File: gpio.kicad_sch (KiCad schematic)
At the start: 3 parts, among them J3 Pyro Connectors

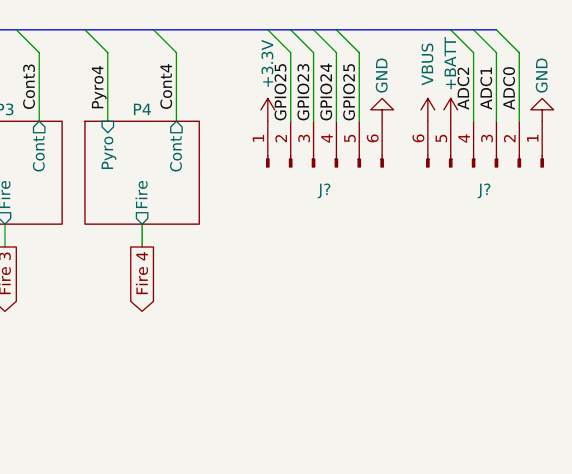
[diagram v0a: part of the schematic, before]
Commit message: Connected the sensors, flash chip, Need to connect the radio and GPS
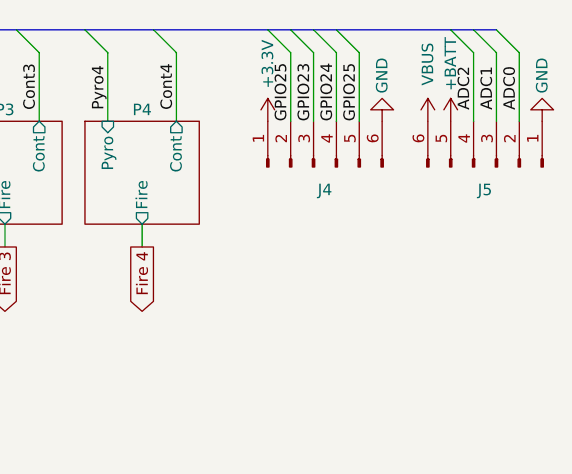
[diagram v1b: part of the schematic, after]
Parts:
- gave numbers to parts that had none: 2
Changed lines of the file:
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@@
   (symbol (lib_id "power:+BATT") (at 114.3 31.75 0) (unit 1)
     (in_bom yes) (on_board yes)
-    (property "Reference" "#PWR?" (id 0) (at 114.3 35.56 0)
+    (property "Reference" "#PWR063" (id 0) (at 114.3 35.56 0)
       (effects (font (size 1.27 1.27)) hide)
     )
@@
   (symbol (lib_id "Connector:Conn_01x06_Male") (at 99.06 36.83 90) (unit 1)
     (in_bom yes) (on_board yes) (fields_autoplaced)
-    (property "Reference" "J?" (id 0) (at 100.33 39.37 90))
+    (property "Reference" "J4" (id 0) (at 100.33 39.37 90))
     (property "Value" "Conn_01x05_Male" (id 1) (at 100.33 41.91 90)
       (effects (font (size 1.27 1.27)) hide)
@@
   (symbol (lib_id "power:+3.3V") (at 93.98 31.75 0) (unit 1)
     (in_bom yes) (on_board yes)
-    (property "Reference" "#PWR?" (id 0) (at 93.98 35.56 0)
+    (property "Reference" "#PWR060" (id 0) (at 93.98 35.56 0)
       (effects (font (size 1.27 1.27)) hide)
     )
@@
   (symbol (lib_id "power:+BATT") (at 35.56 104.14 90) (unit 1)
     (in_bom yes) (on_board yes)
-    (property "Reference" "#PWR057" (id 0) (at 39.37 104.14 0)
+    (property "Reference" "#PWR059" (id 0) (at 39.37 104.14 0)
       (effects (font (size 1.27 1.27)) hide)
     )
@@
   (symbol (lib_id "power:GND") (at 124.46 31.75 180) (unit 1)
     (in_bom yes) (on_board yes)
-    (property "Reference" "#PWR?" (id 0) (at 124.46 25.4 0)
+    (property "Reference" "#PWR064" (id 0) (at 124.46 25.4 0)
       (effects (font (size 1.27 1.27)) hide)
     )
@@
   (symbol (lib_id "power:GND") (at 106.68 31.75 180) (unit 1)
     (in_bom yes) (on_board yes)
-    (property "Reference" "#PWR?" (id 0) (at 106.68 25.4 0)
+    (property "Reference" "#PWR061" (id 0) (at 106.68 25.4 0)
       (effects (font (size 1.27 1.27)) hide)
     )
@@
   (symbol (lib_id "power:VBUS") (at 111.76 31.75 0) (unit 1)
     (in_bom yes) (on_board yes)
-    (property "Reference" "#PWR?" (id 0) (at 111.76 35.56 0)
+    (property "Reference" "#PWR062" (id 0) (at 111.76 35.56 0)
       (effects (font (size 1.27 1.27)) hide)
     )
@@
   (symbol (lib_id "Connector:Conn_01x06_Male") (at 119.38 36.83 270) (mirror x) (unit 1)
     (in_bom yes) (on_board yes) (fields_autoplaced)
-    (property "Reference" "J?" (id 0) (at 118.11 39.37 90))
+    (property "Reference" "J5" (id 0) (at 118.11 39.37 90))
     (property "Value" "Conn_01x05_Male" (id 1) (at 119.38 41.91 90)
       (effects (font (size 1.27 1.27)) hide)

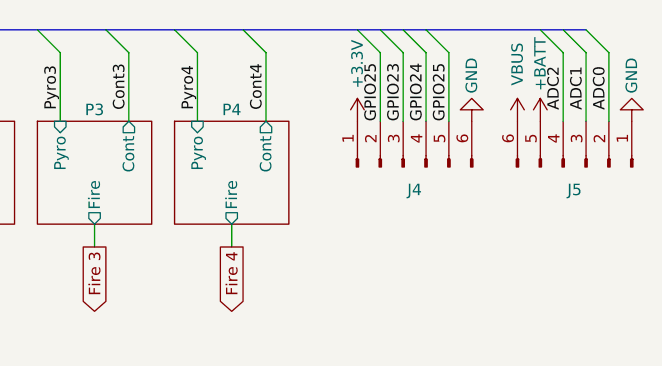
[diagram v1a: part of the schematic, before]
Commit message: Rearranged IO pins to make routing easier. Removed reset, changed BOOTSEL to button
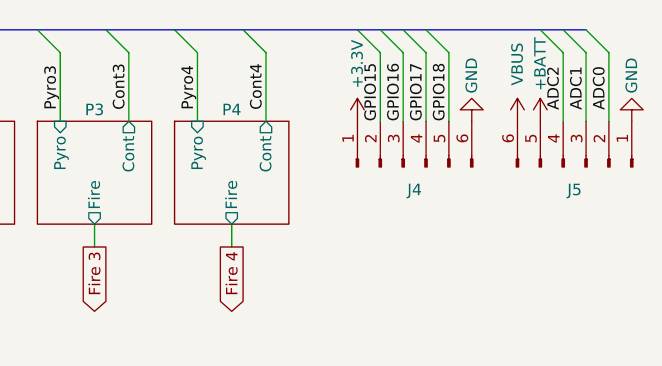
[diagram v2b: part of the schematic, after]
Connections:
- net GPIO23 renamed GPIO16
- net GPIO24 renamed GPIO17
- net GPIO25 renamed GPIO15
- net GPIO15: no longer J4.5 (Pin_5)
- new net GPIO18: J4.5 (Pin_5)
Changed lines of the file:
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@@
+    (effects (font (size 1.27 1.27)) (justify left bottom))
+  )
+  (label "GPIO17" (at 101.6 31.75 90)
+    (effects (font (size 1.27 1.27)) (justify left bottom))
+  )
+  (label "GPIO15" (at 96.52 31.75 90)
     (effects (font (size 1.27 1.27)) (justify left bottom))
   )
@@
     (effects (font (size 1.27 1.27)) (justify left bottom))
   )
-  (label "GPIO25" (at 96.52 31.75 90)
+  (label "GPIO16" (at 99.06 31.75 90)
     (effects (font (size 1.27 1.27)) (justify left bottom))
   )
@@
     (effects (font (size 1.27 1.27)) (justify right bottom))
   )
-  (label "GPIO24" (at 101.6 31.75 90)
-    (effects (font (size 1.27 1.27)) (justify left bottom))
-  )
   (label "Cont1" (at 38.1 30.48 90)
-    (effects (font (size 1.27 1.27)) (justify left bottom))
-  )
-  (label "GPIO25" (at 104.14 31.75 90)
     (effects (font (size 1.27 1.27)) (justify left bottom))
   )
@@
     (effects (font (size 1.27 1.27)) (justify left bottom))
   )
+  (label "GPIO18" (at 104.14 31.75 90)
+    (effects (font (size 1.27 1.27)) (justify left bottom))
+  )
   (label "Cont4" (at 83.82 30.48 90)
     (effects (font (size 1.27 1.27)) (justify left bottom))
   )
-  (label "GPIO23" (at 99.06 31.75 90)
-    (effects (font (size 1.27 1.27)) (justify left bottom))
-  )

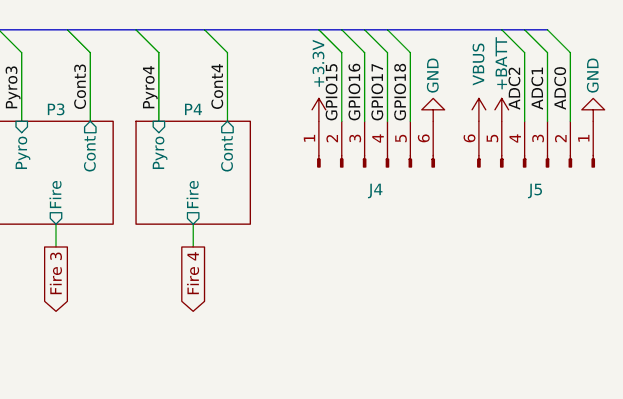
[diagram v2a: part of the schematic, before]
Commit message: Removed GPIO, changed footprints
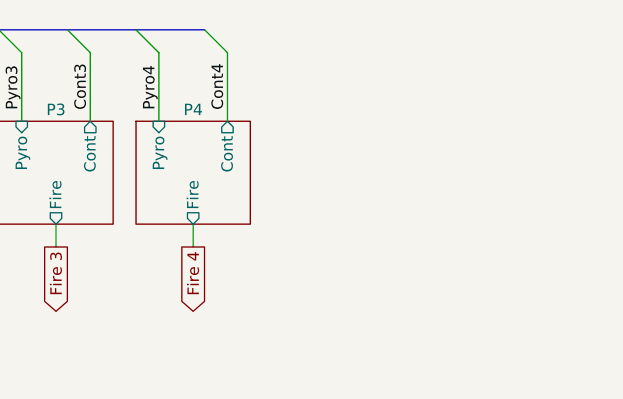
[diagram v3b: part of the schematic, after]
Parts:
- removed J4, J5: Conn_01x05_Male, symbol Connector:Conn_01x06_Male
- J3: footprint Connector_Phoenix_MC_HighVoltage:PhoenixContact_MCV_1,5_10-G-5.08_1x10_P5.08mm_Vertical -> YAR_Connectors:ScrewTerm_2.54x10

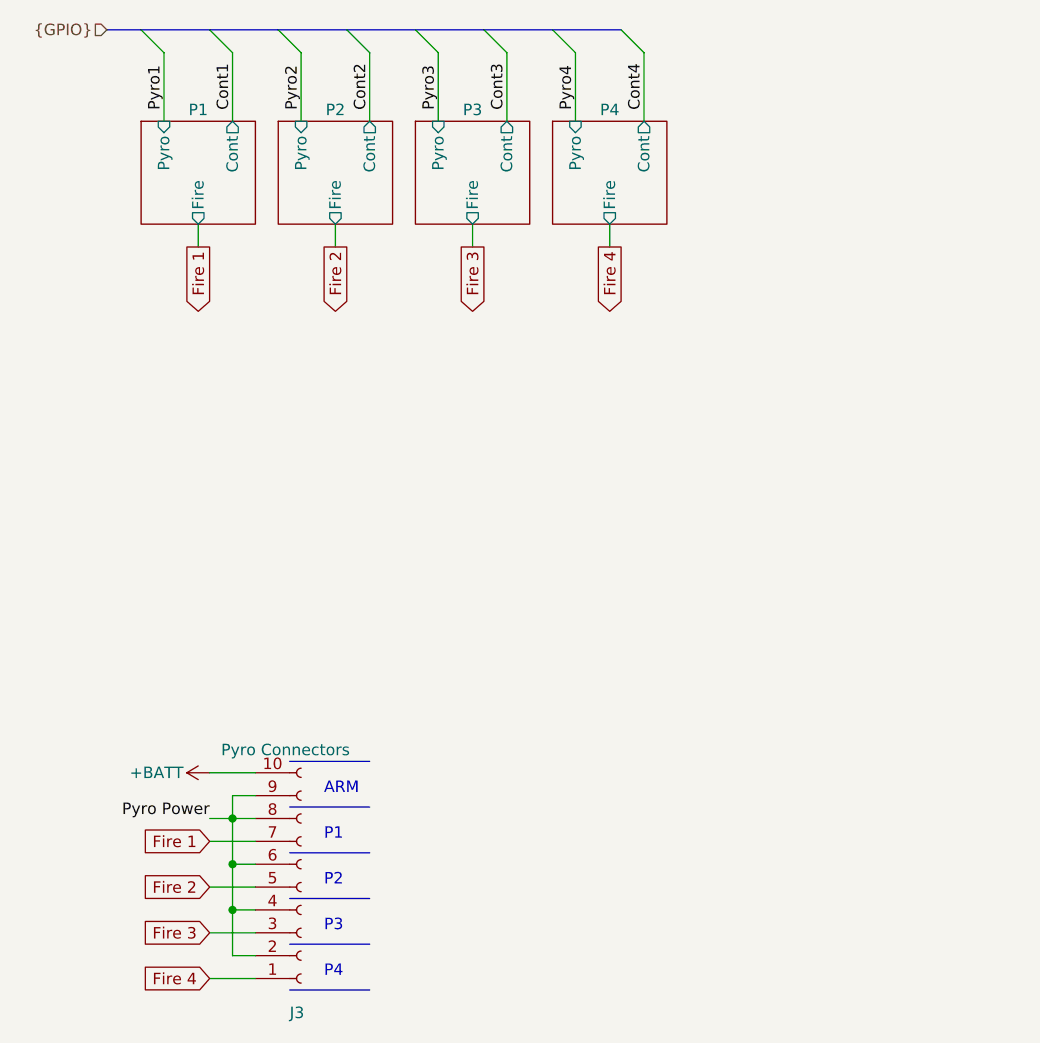
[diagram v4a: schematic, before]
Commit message: Added polyfuse
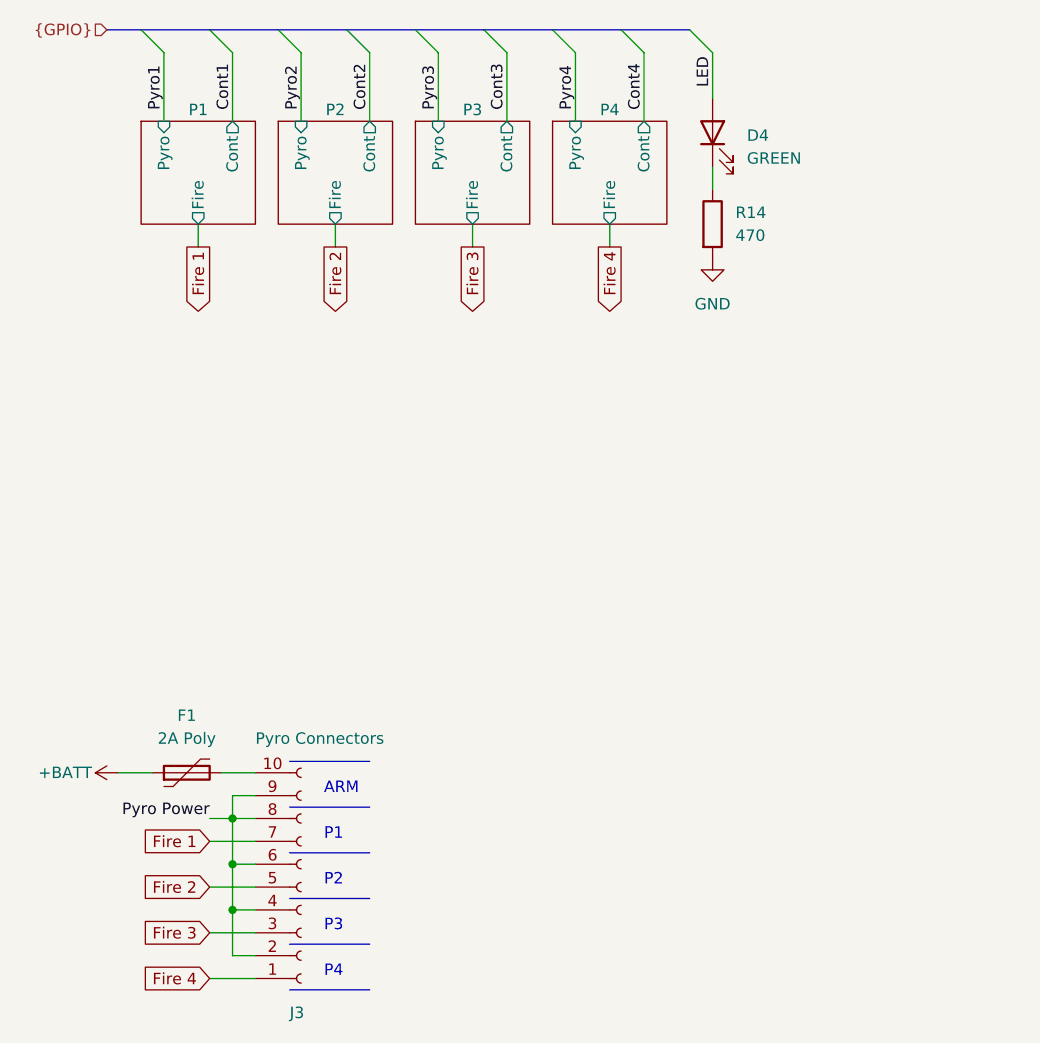
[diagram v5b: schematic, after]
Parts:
- added D4: GREEN, LED_SMD:LED_0603_1608Metric, symbol Device:LED
- added F1: 2A Poly, Fuse:Fuse_0603_1608Metric, symbol Device:Polyfuse
- added R14: 470, Resistor_SMD:R_0603_1608Metric, symbol Device:R
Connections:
- net +BATT: now also F1.1; no longer J3.10 (Pin_10)
- new net: F1.2, J3.10 (Pin_10)
- new net: D4.1 (K), R14.1
- new net GND: R14.2
- new net LED: D4.2 (A)
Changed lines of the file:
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@@
+    (stroke (width 0) (type default) (color 0 0 0 0))
+  )
+  (bus_entry (at 88.9 21.59) (size 2.54 2.54)
     (stroke (width 0) (type default) (color 0 0 0 0))
   )
@@
     (stroke (width 0) (type default) (color 0 0 0 0))
   )
-  (wire (pts (xy 35.56 104.14) (xy 40.64 104.14))
-    (stroke (width 0) (type default) (color 0 0 0 0))
-  )
   (wire (pts (xy 40.64 106.68) (xy 38.1 106.68))
     (stroke (width 0) (type default) (color 0 0 0 0))
@@
     (stroke (width 0) (type default) (color 0 0 0 0))
   )
+  (wire (pts (xy 91.44 39.37) (xy 91.44 36.83))
+    (stroke (width 0) (type default) (color 0 0 0 0))
+  )
   (bus (pts (xy 24.13 21.59) (xy 27.94 21.59))
     (stroke (width 0) (type default) (color 0 0 0 0))
@@
     (stroke (width 0) (type default) (color 0 0 0 0))
   )
+  (bus (pts (xy 81.28 21.59) (xy 88.9 21.59))
+    (stroke (width 0) (type default) (color 0 0 0 0))
+  )
   (wire (pts (xy 35.56 111.76) (xy 40.64 111.76))
     (stroke (width 0) (type default) (color 0 0 0 0))
@@
     (stroke (width 0) (type default) (color 0 0 0 0))
   )
+  (wire (pts (xy 91.44 24.13) (xy 91.44 29.21))
+    (stroke (width 0) (type default) (color 0 0 0 0))
+  )
   (bus (pts (xy 58.42 21.59) (xy 66.04 21.59))
     (stroke (width 0) (type default) (color 0 0 0 0))
@@
   )
   (wire (pts (xy 38.1 119.38) (xy 40.64 119.38))
+    (stroke (width 0) (type default) (color 0 0 0 0))
+  )
+  (wire (pts (xy 36.83 104.14) (xy 40.64 104.14))
+    (stroke (width 0) (type default) (color 0 0 0 0))
+  )
+  (wire (pts (xy 25.4 104.14) (xy 29.21 104.14))
     (stroke (width 0) (type default) (color 0 0 0 0))
   )
@@
   )
   (label "Pyro1" (at 30.48 30.48 90)
+    (effects (font (size 1.27 1.27)) (justify left bottom))
+  )
+  (label "LED" (at 91.44 27.94 90)
     (effects (font (size 1.27 1.27)) (justify left bottom))
   )
@@
       (effects (font (size 1.27 1.27)) (justify left))
     )
-    (property "Value" "Pyro Connectors" (id 1) (at 36.83 101.6 0)
+    (property "Value" "Pyro Connectors" (id 1) (at 40.64 100.33 0)
       (effects (font (size 1.27 1.27)) (justify left))
     )
@@
     (pin "9")
   )
-  (symbol (lib_id "power:+BATT") (at 35.56 104.14 90) (unit 1)
+  (symbol (lib_id "Device:R") (at 91.44 43.18 0) (unit 1)
+    (in_bom yes) (on_board yes) (fields_autoplaced)
+    (property "Reference" "R14" (id 0) (at 93.98 41.9099 0)
+      (effects (font (size 1.27 1.27)) (justify left))
+    )
+    (property "Value" "470" (id 1) (at 93.98 44.4499 0)
+      (effects (font (size 1.27 1.27)) (justify left))
+    )
+    (property "Footprint" "Resistor_SMD:R_0603_1608Metric" (id 2) (at 89.662 43.18 90)
+      (effects (font (size 1.27 1.27)) hide)
+    )
+    (property "Datasheet" "~" (id 3) (at 91.44 43.18 0)
+      (effects (font (size 1.27 1.27)) hide)
+    )
+    (property "JLC" "0603" (id 4) (at 91.44 43.18 0)
+      (effects (font (size 1.27 1.27)) hide)
+    )
+    (property "LCSC" "C22775" (id 5) (at 91.44 43.18 0)
+      (effects (font (size 1.27 1.27)) hide)
+    )
+    (pin "1")
+    (pin "2")
+  )
+  (symbol (lib_id "power:GND") (at 91.44 46.99 0) (unit 1)
+    (in_bom yes) (on_board yes) (fields_autoplaced)
+    (property "Reference" "#PWR058" (id 0) (at 91.44 53.34 0)
+      (effects (font (size 1.27 1.27)) hide)
+    )
+    (property "Value" "GND" (id 1) (at 91.44 52.07 0))
+    (property "Footprint" "" (id 2) (at 91.44 46.99 0)
+      (effects (font (size 1.27 1.27)) hide)
+    )
+    (property "Datasheet" "" (id 3) (at 91.44 46.99 0)
+      (effects (font (size 1.27 1.27)) hide)
+    )
+    (pin "1")
+  )
+  (symbol (lib_id "Device:Polyfuse") (at 33.02 104.14 90) (unit 1)
+    (in_bom yes) (on_board yes) (fields_autoplaced)
+    (property "Reference" "F1" (id 0) (at 33.02 97.79 90))
+    (property "Value" "2A Poly" (id 1) (at 33.02 100.33 90))
+    (property "Footprint" "Fuse:Fuse_0603_1608Metric" (id 2) (at 38.1 102.87 0)
+      (effects (font (size 1.27 1.27)) (justify left) hide)
+    )
+    (property "Datasheet" "~" (id 3) (at 33.02 104.14 0)
+      (effects (font (size 1.27 1.27)) hide)
+    )
+    (pin "1")
+    (pin "2")
+  )
+  (symbol (lib_id "Device:LED") (at 91.44 33.02 90) (unit 1)
+    (in_bom yes) (on_board yes) (fields_autoplaced)
+    (property "Reference" "D4" (id 0) (at 95.25 33.3374 90)
+      (effects (font (size 1.27 1.27)) (justify right))
+    )
+    (property "Value" "GREEN" (id 1) (at 95.25 35.8774 90)
+      (effects (font (size 1.27 1.27)) (justify right))
+    )
+    (property "Footprint" "LED_SMD:LED_0603_1608Metric" (id 2) (at 91.44 33.02 0)
+      (effects (font (size 1.27 1.27)) hide)
+    )
+    (property "Datasheet" "~" (id 3) (at 91.44 33.02 0)
+      (effects (font (size 1.27 1.27)) hide)
+    )
+    (property "JLC" "DNF" (id 4) (at 91.44 33.02 0)
+      (effects (font (size 1.27 1.27)) hide)
+    )
+    (property "LCSC" "DNF" (id 5) (at 91.44 33.02 0)
+      (effects (font (size 1.27 1.27)) hide)
+    )
+    (pin "1")
+    (pin "2")
+  )
+  (symbol (lib_id "power:+BATT") (at 25.4 104.14 90) (unit 1)
     (in_bom yes) (on_board yes)
-    (property "Reference" "#PWR059" (id 0) (at 39.37 104.14 0)
-      (effects (font (size 1.27 1.27)) hide)
-    )
-    (property "Value" "+BATT" (id 1) (at 26.67 104.14 90)
+    (property "Reference" "#PWR057" (id 0) (at 29.21 104.14 0)
+      (effects (font (size 1.27 1.27)) hide)
+    )
+    (property "Value" "+BATT" (id 1) (at 16.51 104.14 90)
       (effects (font (size 1.27 1.27)) (justify right))
     )
-    (property "Footprint" "" (id 2) (at 35.56 104.14 0)
-      (effects (font (size 1.27 1.27)) hide)
-    )
-    (property "Datasheet" "" (id 3) (at 35.56 104.14 0)
-      (effects (font (size 1.27 1.27)) hide)
-    )
+    (property "Footprint" "" (id 2) (at 25.4 104.14 0)
+      (effects (font (size 1.27 1.27)) hide)
+    )
+    (property "Datasheet" "" (id 3) (at 25.4 104.14 0)
+      (effects (font (size 1.27 1.27)) hide)
+    )
